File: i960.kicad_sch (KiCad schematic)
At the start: 51 parts

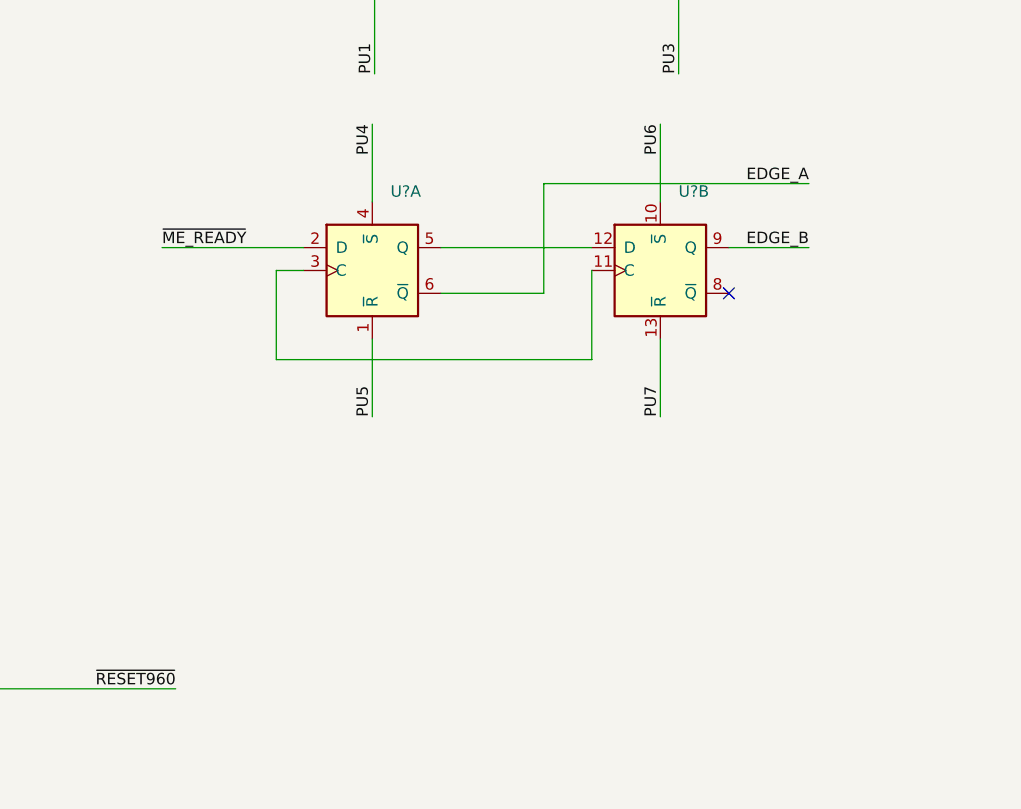
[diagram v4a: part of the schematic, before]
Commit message: Added the jumper block
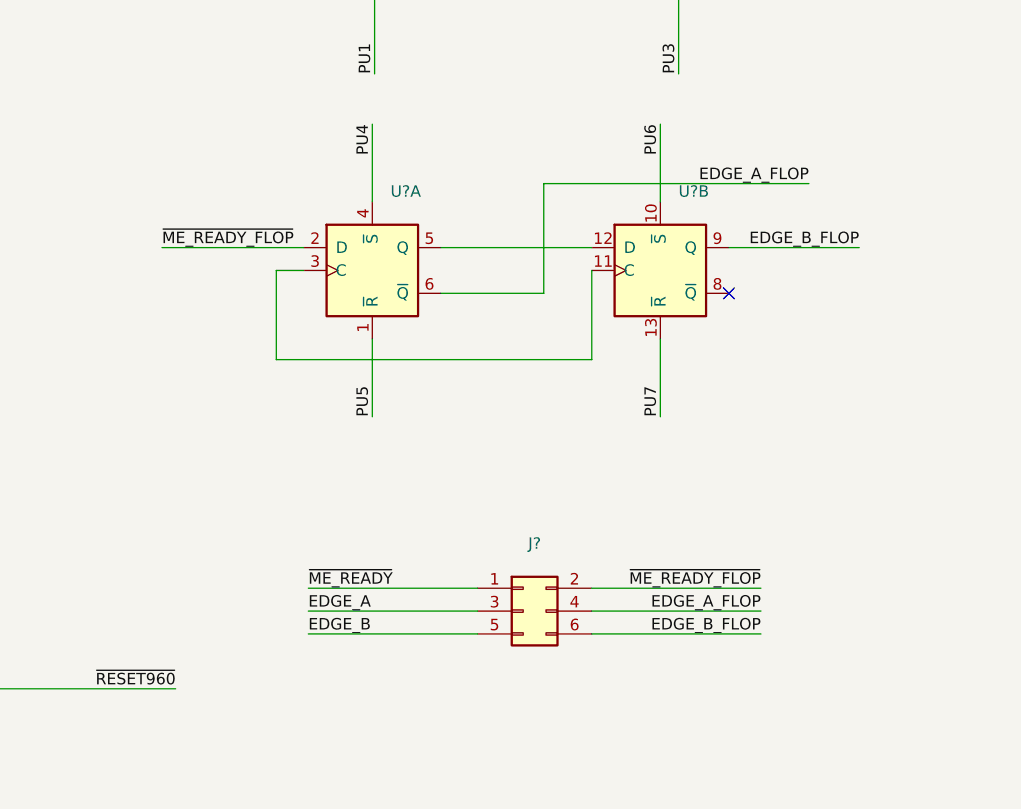
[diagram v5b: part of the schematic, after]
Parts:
- added J?: (no value), symbol Connector_Generic:Conn_02x03_Odd_Even
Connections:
- net EDGE_A: now also J?.3 (Pin_3); no longer U?.6 (~{Q})
- net EDGE_B: now also J?.5 (Pin_5); no longer U?.9 (Q)
- net ~{ME_READY}: now also J?.1 (Pin_1); no longer U?.2 (D)
- new net EDGE_A_FLOP: J?.4 (Pin_4), U?.6 (~{Q})
- new net EDGE_B_FLOP: J?.6 (Pin_6), U?.9 (Q)
- new net ~{ME_READY_FLOP}: J?.2 (Pin_2), U?.2 (D)
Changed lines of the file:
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@@
     (stroke (width 0) (type default) (color 0 0 0 0))
   )
+  (wire (pts (xy 245.364 126.492) (xy 264.16 126.492))
+    (stroke (width 0) (type default) (color 0 0 0 0))
+  )
+  (wire (pts (xy 213.868 121.412) (xy 232.664 121.412))
+    (stroke (width 0) (type default) (color 0 0 0 0))
+  )
   (wire (pts (xy 442.976 129.794) (xy 470.662 129.794))
     (stroke (width 0) (type default) (color 0 0 0 0))
@@
     (stroke (width 0) (type default) (color 0 0 0 0))
   )
+  (wire (pts (xy 213.868 126.492) (xy 232.664 126.492))
+    (stroke (width 0) (type default) (color 0 0 0 0))
+  )
   (wire (pts (xy 467.106 42.164) (xy 502.92 42.164))
     (stroke (width 0) (type default) (color 0 0 0 0))
@@
     (stroke (width 0) (type default) (color 0 0 0 0))
   )
+  (wire (pts (xy 245.364 123.952) (xy 264.16 123.952))
+    (stroke (width 0) (type default) (color 0 0 0 0))
+  )
   (wire (pts (xy 293.878 345.186) (xy 301.752 345.186))
     (stroke (width 0) (type default) (color 0 0 0 0))
@@
     (stroke (width 0) (type default) (color 0 0 0 0))
   )
+  (wire (pts (xy 213.868 123.952) (xy 232.664 123.952))
+    (stroke (width 0) (type default) (color 0 0 0 0))
+  )
   (wire (pts (xy 529.844 48.26) (xy 529.844 53.086))
     (stroke (width 0) (type default) (color 0 0 0 0))
@@
     (stroke (width 0) (type default) (color 0 0 0 0))
   )
+  (wire (pts (xy 245.364 121.412) (xy 264.16 121.412))
+    (stroke (width 0) (type default) (color 0 0 0 0))
+  )
   (wire (pts (xy 190.246 518.668) (xy 190.246 527.05))
     (stroke (width 0) (type default) (color 0 0 0 0))
@@
     (stroke (width 0) (type default) (color 0 0 0 0))
   )
-  (wire (pts (xy 260.604 83.566) (xy 269.494 83.566))
+  (wire (pts (xy 260.604 83.566) (xy 275.082 83.566))
     (stroke (width 0) (type default) (color 0 0 0 0))
   )
@@
     (effects (font (size 1.27 1.27)) (justify right bottom))
   )
+  (label "EDGE_B_FLOP" (at 264.16 126.492 180)
+    (effects (font (size 1.27 1.27)) (justify right bottom))
+  )
   (label "GCM4.~{RESET960}" (at 285.496 534.67 0)
     (effects (font (size 1.27 1.27)) (justify left bottom))
@@
     (effects (font (size 1.27 1.27)) (justify right bottom))
   )
+  (label "EDGE_A" (at 213.868 123.952 0)
+    (effects (font (size 1.27 1.27)) (justify left bottom))
+  )
   (label "UPDI_RXD" (at 97.282 346.71 180)
     (effects (font (size 1.27 1.27)) (justify right bottom))
@@
     (effects (font (size 1.27 1.27)) (justify right bottom))
   )
-  (label "EDGE_A" (at 269.494 76.454 180)
+  (label "EDGE_A_FLOP" (at 269.494 76.454 180)
     (effects (font (size 1.27 1.27)) (justify right bottom))
   )
@@
     (effects (font (size 1.27 1.27)) (justify right bottom))
   )
+  (label "~{ME_READY}" (at 213.868 121.412 0)
+    (effects (font (size 1.27 1.27)) (justify left bottom))
+  )
   (label "i960.~{DATA_LINE_EN}" (at 142.494 50.038 180)
     (effects (font (size 1.27 1.27)) (justify right bottom))
@@
     (effects (font (size 1.27 1.27)) (justify right bottom))
   )
+  (label "EDGE_A_FLOP" (at 264.16 123.952 180)
+    (effects (font (size 1.27 1.27)) (justify right bottom))
+  )
   (label "i960.D1" (at 470.662 104.394 180)
     (effects (font (size 1.27 1.27)) (justify right bottom))
@@
     (effects (font (size 1.27 1.27)) (justify right bottom))
   )
+  (label "EDGE_B" (at 213.868 126.492 0)
+    (effects (font (size 1.27 1.27)) (justify left bottom))
+  )
   (label "AD8" (at 489.966 191.262 0)
     (effects (font (size 1.27 1.27)) (justify left bottom))
@@
     (effects (font (size 1.27 1.27)) (justify right bottom))
   )
-  (label "~{ME_READY}" (at 197.612 83.566 0)
+  (label "~{ME_READY_FLOP}" (at 197.612 83.566 0)
     (effects (font (size 1.27 1.27)) (justify left bottom))
   )
@@
     (effects (font (size 1.27 1.27)) (justify left bottom))
   )
+  (label "~{ME_READY_FLOP}" (at 264.16 121.412 180)
+    (effects (font (size 1.27 1.27)) (justify right bottom))
+  )
   (label "EDGE_A" (at 142.494 91.948 180)
     (effects (font (size 1.27 1.27)) (justify right bottom))
   )
-  (label "EDGE_B" (at 269.494 83.566 180)
+  (label "EDGE_B_FLOP" (at 275.082 83.566 180)
     (effects (font (size 1.27 1.27)) (justify right bottom))
   )
@@
     (pin "9")
   )
+  (symbol (lib_id "Connector_Generic:Conn_02x03_Odd_Even") (at 237.744 123.952 0) (unit 1)
+    (in_bom yes) (on_board yes) (fields_autoplaced)
+    (property "Reference" "J?" (id 0) (at 239.014 116.4422 0))
+    (property "Value" "" (id 1) (at 239.014 118.9791 0))
+    (property "Footprint" "" (id 2) (at 237.744 123.952 0)
+      (effects (font (size 1.27 1.27)) hide)
+    )
+    (property "Datasheet" "~" (id 3) (at 237.744 123.952 0)
+      (effects (font (size 1.27 1.27)) hide)
+    )
+    (pin "1")
+    (pin "2")
+    (pin "3")
+    (pin "4")
+    (pin "5")
+    (pin "6")
+  )
   (symbol (lib_id "power:+5V") (at 163.576 507.492 0) (unit 1)

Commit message: More pullup and pulldown resistors
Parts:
- added R4, R5, R6, R7, R8: (no value), symbol Device:R
- added unit 6 of U13
- gave numbers to parts that had none: 3
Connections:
- net +5V: now also C5.1, U17.1 (A->B), U17.20 (VCC), R4.1, R5.1, R7.1
- net GCM4.HLDA: now also U13.12; no longer U4.14 (B4)
- net GCM4.USART_ME_RX: now also U4.14 (B4); no longer U17.18 (B0)
- net GCM4.USART_PIC_RX: now also U4.13 (B5); no longer U17.17 (B1)
- net GND: now also R6.2, R8.2; no longer U17.19 (CE)
- net ME.TX: now also U4.6 (A4); no longer U17.2 (A0)
- net PIC.TX: now also U4.7 (A5); no longer U17.3 (A1)
- net VCC: no longer C5.1, U17.1 (A->B), U17.20 (VCC)
- net i960.HLDA: now also U13.13; no longer U4.6 (A4)
- net i960.INT1: now also U17.17 (B1), R6.1; no longer U14.12 ((AIN3/CCL2-OUT)PD3)
- net i960.INT2: now also U17.16 (B2), R8.1; no longer U14.26 ((AIN13/XDIR2/CCL3-OUT)PF3)
- net i960.~{BOOT_SUCCESSFUL}: no longer U14.27 ((AIN14)PF4)
- net at U13.5: now also U17.15 (B3), R7.2; no longer U14.36 ((XDIR0/SCL/CCL0-OUT)PA3)
- net at U13.9: now also U17.18 (B0), R5.2; no longer U14.4 ((XDIR1/~{SS}_ALT/CCL1-OUT)PC3)
- net PIC.PA7: now reaches U14.40 ((XDIR0_ALT/CLKO/~{SS})PA7)
- net INT2_OUT: now reaches U17.4 (A2)
- net INT2_OUT: now also U14.26 ((AIN13/XDIR2/CCL3-OUT)PF3)
- net ~{INT3}_OUT: now reaches U17.5 (A3)
- net ~{INT3}_OUT: now also U14.36 ((XDIR0/SCL/CCL0-OUT)PA3)
- new net INT1_OUT: U14.12 ((AIN3/CCL2-OUT)PD3), U17.3 (A1)
- new net ~{BUF_ENABLE}: R4.2, U14.27 ((AIN14)PF4), U17.19 (CE)
- new net ~{INT0}_OUT: U14.4 ((XDIR1/~{SS}_ALT/CCL1-OUT)PC3), U17.2 (A0)
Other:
- moved on the sheet: C5, U13C, U13D, U17

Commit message: Added a second inverter ic to allow HOLD and HLDA to be active low
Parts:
- added C6: (no value), symbol Device:C
- added unit 6 of U13
- added unit 7 of U15
- renumbered U13 to U15
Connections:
- net GCM4.HLDA: now also U15.2; no longer U15.12
- net GCM4.HOLD: now also U13.13; no longer U5.6 (A4)
- net GCM4.USART_ME_TX: now also U5.6 (A4); no longer U5.7 (A5)
- net GCM4.USART_PIC_TX: now also U5.7 (A5); no longer U5.8 (A6)
- net GND: now also C6.2, U15.7 (GND)
- net ME.RX: now also U5.14 (B4); no longer U5.13 (B5)
- net PIC.RX: now also U5.13 (B5); no longer U5.12 (B6)
- net VCC: now also C6.1, U15.14 (VCC)
- net i960.CLK: now also U10.11 (C), U10.3 (C)
- net i960.HLDA: now also U15.1; no longer U15.13
- net i960.HOLD: now also U13.12; no longer U5.14 (B4)
- no-connect marks 6 -> 8
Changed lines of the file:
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@@
   (junction (at 520.954 316.484) (diameter 0) (color 0 0 0 0)
   )
+  (junction (at 262.128 401.066) (diameter 0) (color 0 0 0 0)
+  )
   (junction (at 87.884 298.958) (diameter 0) (color 0 0 0 0)
   )
@@
   (junction (at 34.29 492.76) (diameter 0) (color 0 0 0 0)
   )
+  (junction (at 210.312 86.106) (diameter 0) (color 0 0 0 0)
+  )
   (junction (at 40.64 132.588) (diameter 0) (color 0 0 0 0)
   )
@@
   (junction (at 326.39 569.722) (diameter 0) (color 0 0 0 0)
   )
+  (junction (at 262.128 362.712) (diameter 0) (color 0 0 0 0)
+  )
   (junction (at 169.164 570.738) (diameter 0) (color 0 0 0 0)
   )
@@
   (no_connect (at 24.13 346.71))
   (no_connect (at 23.876 364.236))
+  (no_connect (at 367.284 547.37))
+  (no_connect (at 285.496 547.37))
   (no_connect (at 262.636 46.99))
   (no_connect (at 260.604 88.646))
@@
     (stroke (width 0) (type default) (color 0 0 0 0))
   )
+  (wire (pts (xy 172.974 372.618) (xy 198.882 372.618))
+    (stroke (width 0) (type default) (color 0 0 0 0))
+  )
   (wire (pts (xy 201.676 502.92) (xy 196.088 502.92))
     (stroke (width 0) (type default) (color 0 0 0 0))
@@
     (stroke (width 0) (type default) (color 0 0 0 0))
   )
+  (wire (pts (xy 197.612 86.106) (xy 210.312 86.106))
+    (stroke (width 0) (type default) (color 0 0 0 0))
+  )
   (wire (pts (xy 238.252 271.018) (xy 266.446 271.018))
     (stroke (width 0) (type default) (color 0 0 0 0))
@@
     (stroke (width 0) (type default) (color 0 0 0 0))
   )
+  (wire (pts (xy 262.128 362.712) (xy 280.67 362.712))
+    (stroke (width 0) (type default) (color 0 0 0 0))
+  )
   (wire (pts (xy 102.87 117.348) (xy 142.494 117.348))
     (stroke (width 0) (type default) (color 0 0 0 0))
@@
     (stroke (width 0) (type default) (color 0 0 0 0))
   )
+  (wire (pts (xy 262.128 371.348) (xy 262.128 362.712))
+    (stroke (width 0) (type default) (color 0 0 0 0))
+  )
   (wire (pts (xy 239.776 455.168) (xy 263.398 455.168))
     (stroke (width 0) (type default) (color 0 0 0 0))
@@
     (stroke (width 0) (type default) (color 0 0 0 0))
   )
+  (wire (pts (xy 280.67 386.588) (xy 280.67 401.066))
+    (stroke (width 0) (type default) (color 0 0 0 0))
+  )
   (wire (pts (xy 150.114 278.638) (xy 189.738 278.638))
     (stroke (width 0) (type default) (color 0 0 0 0))
@@
     (stroke (width 0) (type default) (color 0 0 0 0))
   )
+  (wire (pts (xy 280.67 401.066) (xy 262.128 401.066))
+    (stroke (width 0) (type default) (color 0 0 0 0))
+  )
   (wire (pts (xy 258.572 288.798) (xy 266.446 288.798))
     (stroke (width 0) (type default) (color 0 0 0 0))
@@
     (stroke (width 0) (type default) (color 0 0 0 0))
   )
+  (wire (pts (xy 262.128 401.066) (xy 262.128 396.748))
+    (stroke (width 0) (type default) (color 0 0 0 0))
+  )
   (wire (pts (xy 337.312 36.068) (xy 341.63 36.068))
     (stroke (width 0) (type default) (color 0 0 0 0))
@@
     (stroke (width 0) (type default) (color 0 0 0 0))
   )
+  (wire (pts (xy 214.122 372.618) (xy 228.6 372.618))
+    (stroke (width 0) (type default) (color 0 0 0 0))
+  )
   (wire (pts (xy 466.852 286.766) (xy 508 286.766))
     (stroke (width 0) (type default) (color 0 0 0 0))
@@
     (stroke (width 0) (type default) (color 0 0 0 0))
   )
+  (wire (pts (xy 280.67 362.712) (xy 280.67 378.968))
+    (stroke (width 0) (type default) (color 0 0 0 0))
+  )
   (wire (pts (xy 105.918 525.78) (xy 105.918 534.416))
     (stroke (width 0) (type default) (color 0 0 0 0))
@@
     (effects (font (size 1.27 1.27)) (justify left bottom))
   )
-  (label "ME.RX" (at 367.284 544.83 180)
+  (label "ME.RX" (at 367.284 542.29 180)
     (effects (font (size 1.27 1.27)) (justify right bottom))
   )
@@
     (effects (font (size 1.27 1.27)) (justify right bottom))
   )
+  (label "i960.CLK" (at 197.612 86.106 0)
+    (effects (font (size 1.27 1.27)) (justify left bottom))
+  )
   (label "i960.~{INT0}" (at 554.736 530.352 90)
     (effects (font (size 1.27 1.27)) (justify left bottom))
@@
     (effects (font (size 1.27 1.27)) (justify right bottom))
   )
-  (label "i960.HOLD" (at 367.284 542.29 180)
+  (label "i960.HOLD" (at 228.6 372.618 180)
     (effects (font (size 1.27 1.27)) (justify right bottom))
   )
@@
     (effects (font (size 1.27 1.27)) (justify right bottom))
   )
-  (label "GCM4.USART_ME_TX" (at 285.496 544.83 0)
+  (label "GCM4.USART_ME_TX" (at 285.496 542.29 0)
     (effects (font (size 1.27 1.27)) (justify left bottom))
   )
@@
     (effects (font (size 1.27 1.27)) (justify right bottom))
   )
-  (label "GCM4.HOLD" (at 285.496 542.29 0)
+  (label "GCM4.HOLD" (at 172.974 372.618 0)
     (effects (font (size 1.27 1.27)) (justify left bottom))
   )
@@
     (effects (font (size 1.27 1.27)) (justify right bottom))
   )
-  (label "PIC.RX" (at 367.284 547.37 180)
+  (label "PIC.RX" (at 367.284 544.83 180)
     (effects (font (size 1.27 1.27)) (justify right bottom))
   )
@@
     (effects (font (size 1.27 1.27)) (justify left bottom))
   )
-  (label "GCM4.USART_PIC_TX" (at 285.496 547.37 0)
+  (label "GCM4.USART_PIC_TX" (at 285.496 544.83 0)
     (effects (font (size 1.27 1.27)) (justify left bottom))
   )
@@
     (pin "74")
   )
+  (symbol (lib_id "74xx:74AHC04") (at 262.128 384.048 0) (unit 7)
+    (in_bom yes) (on_board yes) (fields_autoplaced)
+    (property "Reference" "U15" (id 0) (at 267.97 383.2133 0)
+      (effects (font (size 1.27 1.27)) (justify left))
+    )
+    (property "Value" "" (id 1) (at 267.97 385.7502 0)
+      (effects (font (size 1.27 1.27)) (justify left))
+    )
+    (property "Footprint" "" (id 2) (at 262.128 384.048 0)
+      (effects (font (size 1.27 1.27)) hide)
+    )
+    (property "Datasheet" "https://assets.nexperia.com/documents/data-sheet/74AHC_AHCT04.pdf" (id 3) (at 262.128 384.048 0)
+      (effects (font (size 1.27 1.27)) hide)
+    )
+    (pin "1")
+    (pin "2")
+    (pin "3")
+    (pin "4")
+    (pin "5")
+    (pin "6")
+    (pin "8")
+    (pin "9")
+    (pin "10")
+    (pin "11")
+    (pin "12")
+    (pin "13")
+    (pin "14")
+    (pin "7")
+  )
   (symbol (lib_id "power:GND") (at 35.052 142.748 0) (unit 1)
     (in_bom yes) (on_board yes) (fields_autoplaced)
@@
     (pin "1")
   )
+  (symbol (lib_id "power:VCC") (at 262.128 362.712 0) (unit 1)
+    (in_bom yes) (on_board yes) (fields_autoplaced)
+    (property "Reference" "#PWR019" (id 0) (at 262.128 366.522 0)
+      (effects (font (size 1.27 1.27)) hide)
+    )
+    (property "Value" "" (id 1) (at 262.128 359.1362 0))
+    (property "Footprint" "" (id 2) (at 262.128 362.712 0)
+      (effects (font (size 1.27 1.27)) hide)
+    )
+    (property "Datasheet" "" (id 3) (at 262.128 362.712 0)
+      (effects (font (size 1.27 1.27)) hide)
+    )
+    (pin "1")
+  )
   (symbol (lib_id "NewICs:i960Sx_PLCC84") (at 553.72 101.854 0) (unit 2)
     (in_bom yes) (on_board yes) (fields_autoplaced)
@@
     (pin "1")
   )
+  (symbol (lib_id "74xx:74AHC04") (at 206.502 372.618 0) (unit 6)
+    (in_bom yes) (on_board yes) (fields_autoplaced)
+    (property "Reference" "U13" (id 0) (at 206.502 365.1082 0))
+    (property "Value" "" (id 1) (at 206.502 367.6451 0))
+    (property "Footprint" "" (id 2) (at 206.502 372.618 0)
+      (effects (font (size 1.27 1.27)) hide)
+    )
+    (property "Datasheet" "https://assets.nexperia.com/documents/data-sheet/74AHC_AHCT04.pdf" (id 3) (at 206.502 372.618 0)
+      (effects (font (size 1.27 1.27)) hide)
+    )
+    (pin "1")
+    (pin "2")
+    (pin "3")
+    (pin "4")
+    (pin "5")
+    (pin "6")
+    (pin "8")
+    (pin "9")
+    (pin "10")
+    (pin "11")
+    (pin "12")
+    (pin "13")
+    (pin "14")
+    (pin "7")
+  )
   (symbol (lib_id "Device:C") (at 496.316 537.464 0) (unit 1)
     (in_bom yes) (on_board yes) (fields_autoplaced)
@@
     (pin "74")
   )
+  (symbol (lib_id "power:GND") (at 262.128 401.066 0) (unit 1)
+    (in_bom yes) (on_board yes) (fields_autoplaced)
+    (property "Reference" "#PWR020" (id 0) (at 262.128 407.416 0)
+      (effects (font (size 1.27 1.27)) hide)
+    )
+    (property "Value" "" (id 1) (at 262.128 405.5094 0))
+    (property "Footprint" "" (id 2) (at 262.128 401.066 0)
+      (effects (font (size 1.27 1.27)) hide)
+    )
+    (property "Datasheet" "" (id 3) (at 262.128 401.066 0)
+      (effects (font (size 1.27 1.27)) hide)
+    )
+    (pin "1")
+  )
   (symbol (lib_id "Device:C") (at 28.448 545.338 0) (unit 1)
     (in_bom yes) (on_board yes) (fields_autoplaced)
@@
     (pin "2")
   )
+  (symbol (lib_id "Device:C") (at 280.67 382.778 0) (unit 1)
+    (in_bom yes) (on_board yes) (fields_autoplaced)
+    (property "Reference" "C6" (id 0) (at 283.591 381.9433 0)
+      (effects (font (size 1.27 1.27)) (justify left))
+    )
+    (property "Value" "" (id 1) (at 283.591 384.4802 0)
+      (effects (font (size 1.27 1.27)) (justify left))
+    )
+    (property "Footprint" "" (id 2) (at 281.6352 386.588 0)
+      (effects (font (size 1.27 1.27)) hide)
+    )
+    (property "Datasheet" "~" (id 3) (at 280.67 382.778 0)
+      (effects (font (size 1.27 1.27)) hide)
+    )
+    (pin "1")
+    (pin "2")
+  )
   (symbol (lib_id "power:GND") (at 520.954 370.586 0) (unit 1)
     (in_bom yes) (on_board yes) (fields_autoplaced)
@@
     (pin "2")
   )
-  (symbol (lib_id "74xx:74AHC04") (at 206.248 361.188 0) (unit 6)
+  (symbol (lib_id "74xx:74AHC04") (at 206.248 361.188 0) (unit 1)
     (in_bom yes) (on_board yes) (fields_autoplaced)
-    (property "Reference" "U13" (id 0) (at 206.248 353.6782 0))
+    (property "Reference" "U15" (id 0) (at 206.248 353.6782 0))
     (property "Value" "" (id 1) (at 206.248 356.2151 0))
     (property "Footprint" "" (id 2) (at 206.248 361.188 0)

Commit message: Use an AHC157 for the deactivation of the interrupt lines while changes are being made to the CCLs
Instead of using tons of pullups and downs, use the AHC157 channel
feature. Channel 0 is the connection between CCLS and i960. Channel 1 is
a fixed pattern that is useful for booting and deactivating all
interrupts
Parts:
- removed R5, R6, R7, R8: (no value), symbol Device:R
- removed U17: (no value), symbol 74xx:74HC245
- added U17: (no value), symbol 74xx:74LS157
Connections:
- net +5V: now also U17.13 (I1d), U17.16 (VCC), U17.3 (I1a)
- net GND: now also U17.10 (I1c), U17.15 (E), U17.6 (I1b), U17.8 (GND)
- net INT1_OUT: now also U17.5 (I0b)
- net INT2_OUT: now also U17.11 (I0c)
- net i960.INT1: now also U17.7 (Zb)
- net i960.INT2: now also U17.9 (Zc)
- net i960.~{INT0}: now also U17.4 (Za); no longer U13.8
- net i960.~{INT3}: now also U17.12 (Zd); no longer U13.6
- net ~{BUF_ENABLE}: now also U17.1 (S)
- net ~{INT0}_OUT: now also U13.8, U17.2 (I0a); no longer U14.4 ((XDIR1/~{SS}_ALT/CCL1-OUT)PC3)
- net ~{INT3}_OUT: now also U13.6, U17.14 (I0d); no longer U14.36 ((XDIR0/SCL/CCL0-OUT)PA3)
- net at U13.9: now also U14.4 ((XDIR1/~{SS}_ALT/CCL1-OUT)PC3)
- net at U13.5: now also U14.36 ((XDIR0/SCL/CCL0-OUT)PA3)
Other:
- moved on the sheet: R2, R3, R4, U13C, U13D
